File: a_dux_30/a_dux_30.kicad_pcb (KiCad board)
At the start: 2 copper layers, 118.9 x 97.9 mm, 32 parts

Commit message: add routes and img
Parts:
- added G***: LOGO, imgs:felix_dazed, F.Cu at (53.1, -4.99)
- added G***: LOGO, imgs:felix_love, B.Cu at (52.7, -5.32)
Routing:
- net GND: track 0.00 -> 712.3 mm
- net P5: track 0.00 -> 159.3 mm
- net P2: track 0.00 -> 155.3 mm
- net P6: track 0.00 -> 143.3 mm
- net P3: track 0.00 -> 136.4 mm
- net P4: track 0.00 -> 125.2 mm
- net P14: track 0.00 -> 118.7 mm
- net P16: track 0.00 -> 101.8 mm
- net P19: track 0.00 -> 89.4 mm
- net P10: track 0.00 -> 84.5 mm
- net P8: track 0.00 -> 80.9 mm
- net P7: track 0.00 -> 80.5 mm
- net P18: track 0.00 -> 70.7 mm
- net P15: track 0.00 -> 61.6 mm
- net P20: track 0.00 -> 39.9 mm
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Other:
- net class Default removed

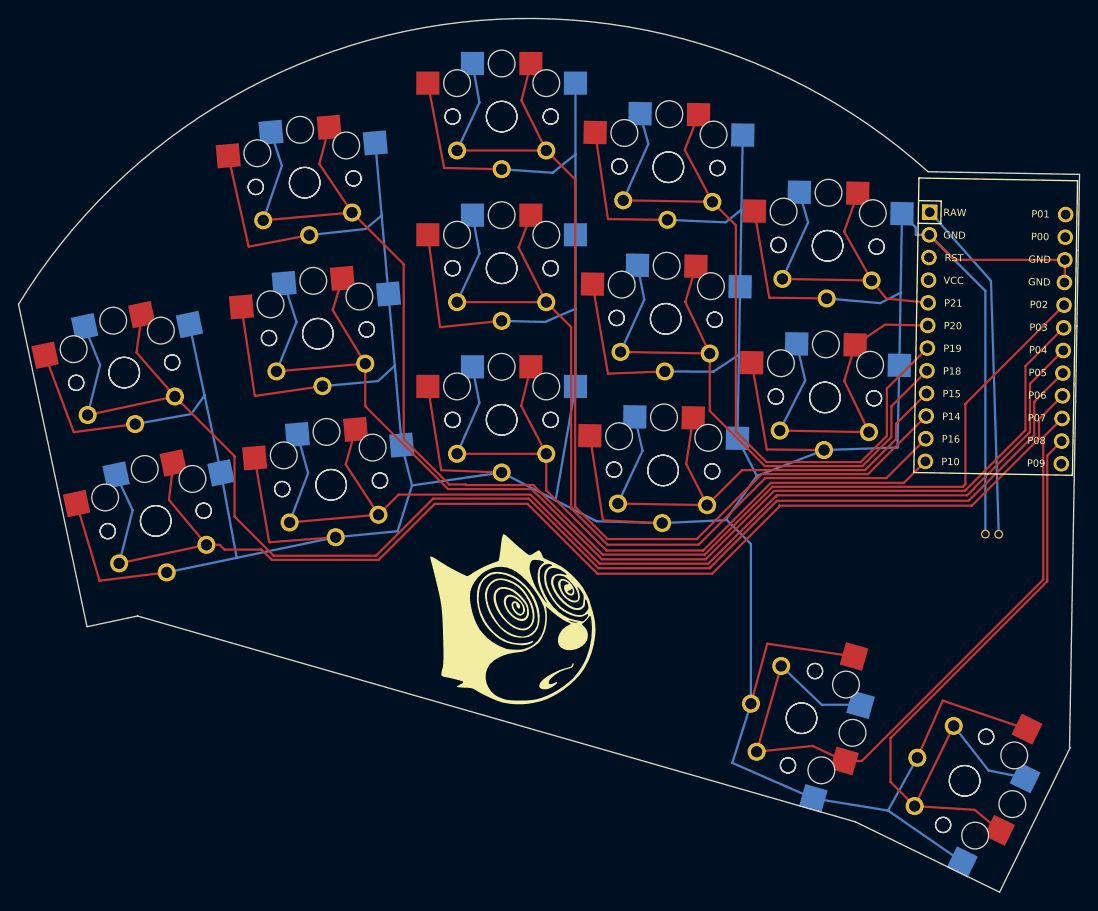
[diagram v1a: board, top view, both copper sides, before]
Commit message: add teardrops
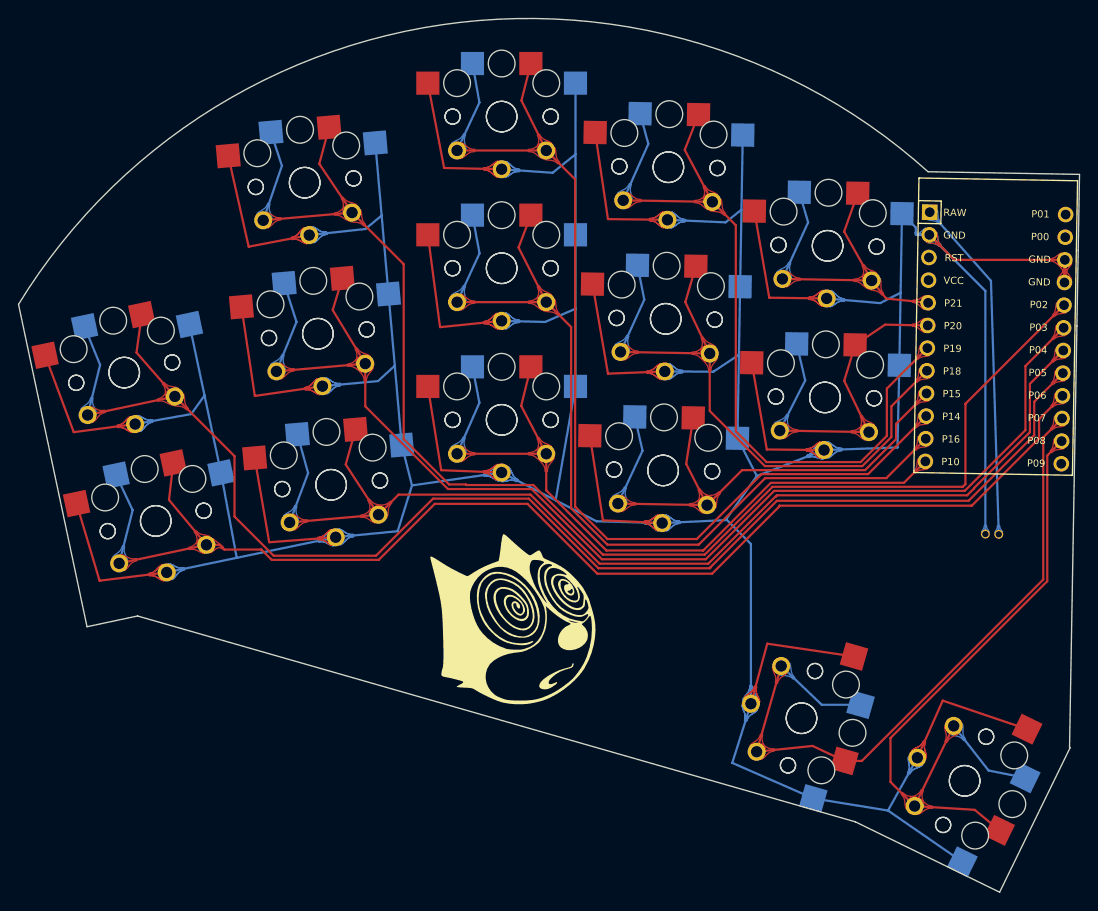
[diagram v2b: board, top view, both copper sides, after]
